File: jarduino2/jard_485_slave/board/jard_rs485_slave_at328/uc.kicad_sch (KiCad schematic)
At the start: 13 parts, among them J7 ISCP, U5 ATmega328P-A, Y1 Resonator

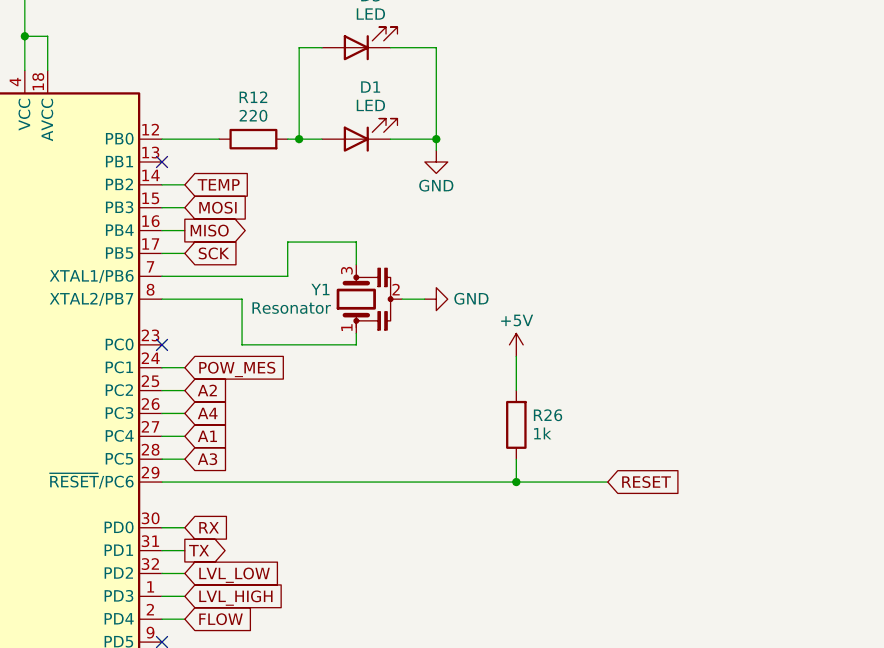
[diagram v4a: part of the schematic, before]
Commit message: Correction empreinte résonateur
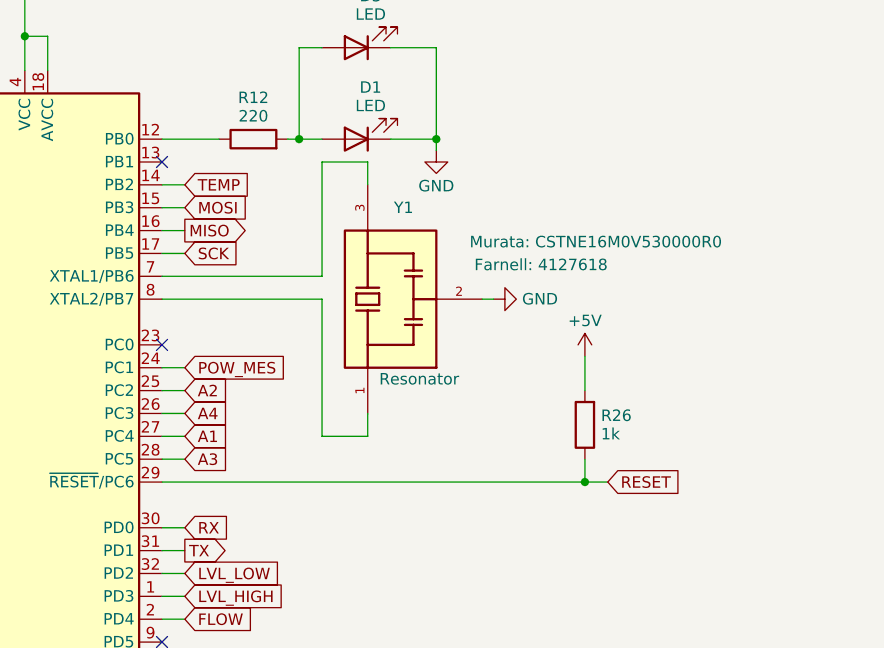
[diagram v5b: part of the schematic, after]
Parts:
- U5: Fabricant (none) -> Microchip: ATMEGA328P-AN; Fournisseur (none) -> Farnell: 2443178
- Y1: footprint Crystal:Resonator_SMD_Murata_CSTxExxV-3Pin_3.0x1.1mm_HandSoldering -> bpc:BPC_16MHz_CSTNE16M0V530000R0; symbol Device:Resonator -> bpc:BPC_16MHz_CSTNE16M0V530000R0; Availability (none) -> In Stock; Check_prices (none) -> https://www.snapeda.com/parts/CSTNE16M0V530000R0/Murata+Ele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; Fabricant (none) -> Murata: CSTNE16M0V530000R0; Fournisseur (none) -> Farnell: 4127618; MANUFACTURER (none) -> Murata; MAXIMUM_PACKAGE_HEIGHT (none) -> 1mm; MF (none) -> Murata Electronics; MP (none) -> CSTNE16M0V530000R0; PARTREV (none) -> JGC42-8853B; Package (none) -> SMD-3 Murata; Price (none) -> None; Purchase-URL (none) -> https://www.snapeda.com/api/url_track_click_mouser/?unipart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; STANDARD (none) -> Manufacturer Recomendations; SnapEDA_Link (none) -> https://www.snapeda.com/parts/CSTNE16M0V530000R0/Murata+Ele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
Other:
- moved on the sheet: R26

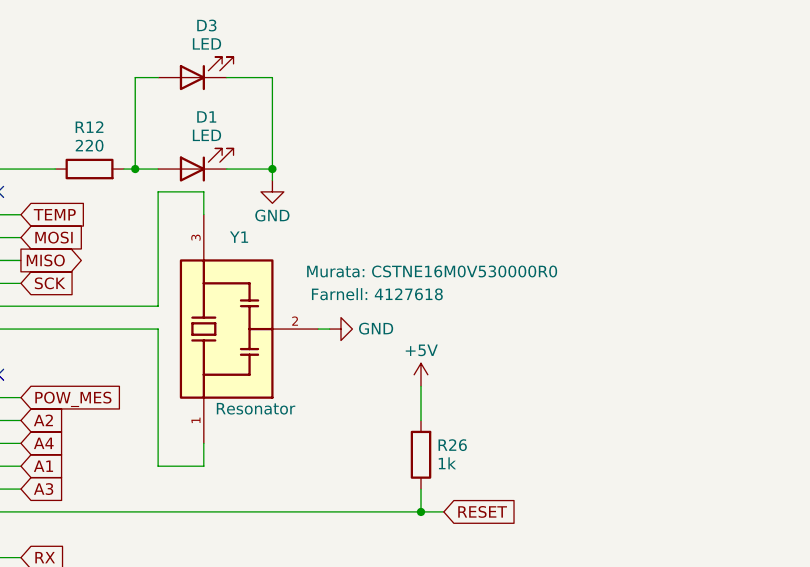
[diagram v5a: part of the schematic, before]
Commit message: Correction erreur de MOS (N au lieu de P) + Saisie complete de la BOM
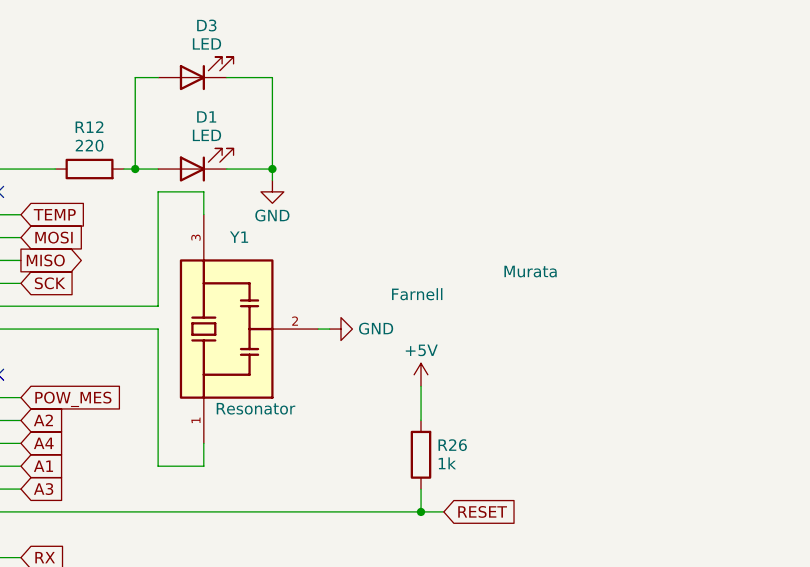
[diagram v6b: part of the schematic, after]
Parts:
- C? (x5): Fabricant (none) -> KEMET; Fournisseur (none) -> Farnell; RefFabricant (none) -> C0603X102J5GACAUTO; RefFournisseur (none) -> 2219417
- D1: Fabricant (none) -> ROHM; Fournisseur (none) -> Farnell; RefFabricant (none) -> SML-D14VWT86C; RefFournisseur (none) -> 2829438
- J7: Fabricant (none) -> AMPHENOL; Fournisseur (none) -> Farnell; RefFabricant (none) -> 95278-101-06LF; RefFournisseur (none) -> 3882224
- R12: Fabricant (none) -> MULTICOMP PRO; Fournisseur (none) -> Farnell; RefFabricant (none) -> MCMR06X224 JTL; RefFournisseur (none) -> 2073437
- R26: Fabricant (none) -> MULTICOMP PRO; Fournisseur (none) -> Farnell; RefFabricant (none) -> MC0100W060311K; RefFournisseur (none) -> 2845750
- U5: Fabricant Microchip: ATMEGA328P-AN -> Microchip; Fournisseur Farnell: 2443178 -> Farnell; RefFabricant (none) -> ATMEGA328P-AN; RefFournisseur (none) -> 2443178
- Y1: Fabricant Murata: CSTNE16M0V530000R0 -> Murata; Fournisseur Farnell: 4127618 -> Farnell; RefFabricant (none) -> CSTNE16M0V530000R0; RefFournisseur (none) -> 4127618
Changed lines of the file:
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@@
   (title_block
     (title "Carte de commande d'un OYA - Esclave RS485")
-    (date "2024-04-01")
-    (rev "D0")
+    (date "2024-04-02")
+    (rev "E0")
     (company "BPC")
     (comment 1 "Technologie CMS basée sur ATMEGA328")
@@
       (effects (font (size 1.27 1.27)) hide)
     )
+    (property "RefFabricant" "C0603X102J5GACAUTO" (at 109.22 95.25 0)
+      (effects (font (size 1.27 1.27)) hide)
+    )
+    (property "RefFournisseur" "2219417" (at 109.22 95.25 0)
+      (effects (font (size 1.27 1.27)) hide)
+    )
+    (property "Fabricant" "KEMET" (at 109.22 95.25 0)
+      (effects (font (size 1.27 1.27)) hide)
+    )
+    (property "Fournisseur" "Farnell" (at 109.22 95.25 0)
+      (effects (font (size 1.27 1.27)) hide)
+    )
+    (property "Description" "Condensateur céramique 100nF" (at 109.22 95.25 0)
+      (effects (font (size 1.27 1.27)) hide)
+    )
     (pin "1")
     (pin "2")
@@
     )
     (property "Datasheet" "~" (at 229.87 63.5 0)
+      (effects (font (size 1.27 1.27)) hide)
+    )
+    (property "RefFabricant" "95278-101-06LF" (at 229.87 63.5 0)
+      (effects (font (size 1.27 1.27)) hide)
+    )
+    (property "RefFournisseur" "3882224" (at 229.87 63.5 0)
+      (effects (font (size 1.27 1.27)) hide)
+    )
+    (property "Fabricant" "AMPHENOL" (at 229.87 63.5 0)
+      (effects (font (size 1.27 1.27)) hide)
+    )
+    (property "Fournisseur" "Farnell" (at 229.87 63.5 0)
+      (effects (font (size 1.27 1.27)) hide)
+    )
+    (property "Description" "Connecteur Header 6 broches" (at 229.87 63.5 0)
       (effects (font (size 1.27 1.27)) hide)
     )
@@
       (effects (font (size 1.27 1.27)) hide)
     )
+    (property "RefFabricant" "C0603X102J5GACAUTO" (at 143.51 69.85 0)
+      (effects (font (size 1.27 1.27)) hide)
+    )
+    (property "RefFournisseur" "2219417" (at 143.51 69.85 0)
+      (effects (font (size 1.27 1.27)) hide)
+    )
+    (property "Fabricant" "KEMET" (at 143.51 69.85 0)
+      (effects (font (size 1.27 1.27)) hide)
+    )
+    (property "Fournisseur" "Farnell" (at 143.51 69.85 0)
+      (effects (font (size 1.27 1.27)) hide)
+    )
+    (property "Description" "Condensateur céramique 100nF" (at 143.51 69.85 0)
+      (effects (font (size 1.27 1.27)) hide)
+    )
     (pin "1")
     (pin "2")
@@
       (effects (font (size 1.27 1.27)) hide)
     )
+    (property "RefFabricant" "C0603X102J5GACAUTO" (at 53.34 158.75 0)
+      (effects (font (size 1.27 1.27)) hide)
+    )
+    (property "RefFournisseur" "2219417" (at 53.34 158.75 0)
+      (effects (font (size 1.27 1.27)) hide)
+    )
+    (property "Fabricant" "KEMET" (at 53.34 158.75 0)
+      (effects (font (size 1.27 1.27)) hide)
+    )
+    (property "Fournisseur" "Farnell" (at 53.34 158.75 0)
+      (effects (font (size 1.27 1.27)) hide)
+    )
+    (property "Description" "Condensateur céramique 1nF" (at 53.34 158.75 0)
+      (effects (font (size 1.27 1.27)) hide)
+    )
     (pin "1")
     (pin "2")
@@
       (effects (font (size 1.27 1.27)) hide)
     )
+    (property "RefFabricant" "MC0100W060311K" (at 195.58 127 0)
+      (effects (font (size 1.27 1.27)) hide)
+    )
+    (property "RefFournisseur" "2845750" (at 195.58 127 0)
+      (effects (font (size 1.27 1.27)) hide)
+    )
+    (property "Fabricant" "MULTICOMP PRO" (at 195.58 127 0)
+      (effects (font (size 1.27 1.27)) hide)
+    )
+    (property "Fournisseur" "Farnell" (at 195.58 127 0)
+      (effects (font (size 1.27 1.27)) hide)
+    )
+    (property "Description" "Résistance 1kOhms" (at 195.58 127 0)
+      (effects (font (size 1.27 1.27)) hide)
+    )
     (pin "1")
     (pin "2")
@@
     )
     (property "Datasheet" "~" (at 170.18 95.25 0)
+      (effects (font (size 1.27 1.27)) hide)
+    )
+    (property "RefFabricant" "SML-D14VWT86C" (at 170.18 95.25 0)
+      (effects (font (size 1.27 1.27)) hide)
+    )
+    (property "RefFournisseur" "2829438" (at 170.18 95.25 0)
+      (effects (font (size 1.27 1.27)) hide)
+    )
+    (property "Fabricant" "ROHM" (at 170.18 95.25 0)
+      (effects (font (size 1.27 1.27)) hide)
+    )
+    (property "Fournisseur" "Farnell" (at 170.18 95.25 0)
+      (effects (font (size 1.27 1.27)) hide)
+    )
+    (property "Description" "LED rouge 805" (at 170.18 95.25 0)
       (effects (font (size 1.27 1.27)) hide)
     )
@@
       (effects (font (size 1.27 1.27)) hide)
     )
-    (property "Fabricant" "Murata: CSTNE16M0V530000R0" (at 210.82 106.68 90)
-      (effects (font (size 1.27 1.27)) (justify left))
-    )
-    (property "Fournisseur" "Farnell: 4127618" (at 198.12 109.22 90)
+    (property "Fabricant" "Murata" (at 210.82 106.68 90)
+      (effects (font (size 1.27 1.27)) (justify left))
+    )
+    (property "Fournisseur" "Farnell" (at 198.12 109.22 90)
       (effects (font (size 1.27 1.27)) (justify left))
     )
@@
       (effects (font (size 1.27 1.27)) (justify bottom) hide)
     )
-    (property "Description" "\n16 MHz Ceramic Resonator Built in Capacitor 15 pF ±0.3% 40 Ohms -40°C ~ 85°C Surface Mount\n" (at 173.99 113.03 0)
+    (property "Description" "Résonateur \n16 MHz / 15 pF" (at 173.99 113.03 0)
       (effects (font (size 1.27 1.27)) (justify bottom) hide)
     )
@@
     (property "MANUFACTURER" "Murata" (at 173.99 113.03 0)
       (effects (font (size 1.27 1.27)) (justify bottom) hide)
+    )
+    (property "RefFabricant" "CSTNE16M0V530000R0" (at 173.99 113.03 0)
+      (effects (font (size 1.27 1.27)) hide)
+    )
+    (property "RefFournisseur" "4127618" (at 173.99 113.03 0)
+      (effects (font (size 1.27 1.27)) hide)
     )
     (pin "1")
@@
     )
     (property "Datasheet" "" (at 49.53 161.29 0)
+      (effects (font (size 1.27 1.27)) hide)
+    )
+    (property "RefFabricant" "" (at 49.53 163.83 0)
+      (effects (font (size 1.27 1.27)) hide)
+    )
+    (property "RefFournisseur" "" (at 49.53 163.83 0)
+      (effects (font (size 1.27 1.27)) hide)
+    )
+    (property "Description" "Module de température Arduino" (at 49.53 163.83 0)
       (effects (font (size 1.27 1.27)) hide)
     )
@@
       (effects (font (size 1.27 1.27)) hide)
     )
-    (property "Fabricant" "Microchip: ATMEGA328P-AN" (at 133.35 125.73 0)
-      (effects (font (size 1.27 1.27)) hide)
-    )
-    (property "Fournisseur" "Farnell: 2443178" (at 133.35 125.73 0)
+    (property "Fabricant" "Microchip" (at 133.35 125.73 0)
+      (effects (font (size 1.27 1.27)) hide)
+    )
+    (property "Fournisseur" "Farnell" (at 133.35 125.73 0)
+      (effects (font (size 1.27 1.27)) hide)
+    )
+    (property "RefFabricant" "ATMEGA328P-AN" (at 133.35 125.73 0)
+      (effects (font (size 1.27 1.27)) hide)
+    )
+    (property "RefFournisseur" "2443178" (at 133.35 125.73 0)
+      (effects (font (size 1.27 1.27)) hide)
+    )
+    (property "Description" "Microcontrolleur ATMEGA328P" (at 133.35 125.73 0)
       (effects (font (size 1.27 1.27)) hide)
     )
@@
       (effects (font (size 1.27 1.27)) hide)
     )
+    (property "RefFabricant" "C0603X102J5GACAUTO" (at 143.51 58.42 0)
+      (effects (font (size 1.27 1.27)) hide)
+    )
+    (property "RefFournisseur" "2219417" (at 143.51 58.42 0)
+      (effects (font (size 1.27 1.27)) hide)
+    )
+    (property "Fabricant" "KEMET" (at 143.51 58.42 0)
+      (effects (font (size 1.27 1.27)) hide)
+    )
+    (property "Fournisseur" "Farnell" (at 143.51 58.42 0)
+      (effects (font (size 1.27 1.27)) hide)
+    )
+    (property "Description" "Condensateur céramique 1nF" (at 143.51 58.42 0)
+      (effects (font (size 1.27 1.27)) hide)
+    )
     (pin "1")
     (pin "2")
@@
       (effects (font (size 1.27 1.27)) hide)
     )
+    (property "RefFabricant" "C0603X102J5GACAUTO" (at 143.51 46.99 0)
+      (effects (font (size 1.27 1.27)) hide)
+    )
+    (property "RefFournisseur" "2219417" (at 143.51 46.99 0)
+      (effects (font (size 1.27 1.27)) hide)
+    )
+    (property "Fabricant" "KEMET" (at 143.51 46.99 0)
+      (effects (font (size 1.27 1.27)) hide)
+    )
+    (property "Fournisseur" "Farnell" (at 143.51 46.99 0)
+      (effects (font (size 1.27 1.27)) hide)
+    )
+    (property "Description" "Condensateur céramique 100nF" (at 143.51 46.99 0)
+      (effects (font (size 1.27 1.27)) hide)
+    )
     (pin "1")
     (pin "2")
@@
       (effects (font (size 1.27 1.27)) hide)
     )
+    (property "RefFabricant" "MCMR06X224 JTL" (at 158.75 95.25 0)
+      (effects (font (size 1.27 1.27)) hide)
+    )
+    (property "RefFournisseur" "2073437" (at 158.75 95.25 0)
+      (effects (font (size 1.27 1.27)) hide)
+    )
+    (property "Fabricant" "MULTICOMP PRO" (at 158.75 95.25 0)
+      (effects (font (size 1.27 1.27)) hide)
+    )
+    (property "Fournisseur" "Farnell" (at 158.75 95.25 0)
+      (effects (font (size 1.27 1.27)) hide)
+    )
+    (property "Description" "Résistance 220 Ohms" (at 158.75 95.25 0)
+      (effects (font (size 1.27 1.27)) hide)
+    )
     (pin "1")
     (pin "2")
@@
       (effects (font (size 1.27 1.27)) hide)
     )
+    (property "RefFabricant" "" (at 170.18 85.09 0)
+      (effects (font (size 1.27 1.27)) hide)
+    )
+    (property "RefFournisseur" "" (at 170.18 85.09 0)
+      (effects (font (size 1.27 1.27)) hide)
+    )
+    (property "Description" "LED rouge 3mm" (at 170.18 85.09 0)
+      (effects (font (size 1.27 1.27)) hide)
+    )

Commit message: Ajout des prix des composants
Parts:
- C? (x5): Price (none) -> 0,42
- D1: Price (none) -> 0,4992
- D3: Fabricant (none) -> MULTICOMP PRO; Fournisseur (none) -> Farnell; Price (none) -> 3,78; RefFabricant (none) -> MP000451; RefFournisseur (none) -> 3130206
- J7: Price (none) -> 0,5748
- R12: Price (none) -> 0,009
- R26: Price (none) -> 0,0036
- U5: Price (none) -> 3,12
- U?: Fournisseur (none) -> Ali express; Price (none) -> 0,635; Purchase-URL (none) -> https://fr.aliexpress.com/item/1005005046929046.html?spm=a2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; RefFournisseur (none) -> DTH22
- Y1: Price None -> 0,2616
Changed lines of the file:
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@@
+      (effects (font (size 1.27 1.27)) hide)
+    )
+    (property "Price" "0,42" (at 109.22 95.25 0)
       (effects (font (size 1.27 1.27)) hide)
     )
@@
     )
     (property "Description" "Connecteur Header 6 broches" (at 229.87 63.5 0)
+      (effects (font (size 1.27 1.27)) hide)
+    )
+    (property "Price" "0,5748" (at 229.87 63.5 0)
       (effects (font (size 1.27 1.27)) hide)
     )
@@
       (effects (font (size 1.27 1.27)) hide)
     )
+    (property "Price" "0,42" (at 143.51 69.85 0)
+      (effects (font (size 1.27 1.27)) hide)
+    )
     (pin "1")
     (pin "2")
@@
       (effects (font (size 1.27 1.27)) hide)
     )
+    (property "Price" "0,42" (at 53.34 158.75 0)
+      (effects (font (size 1.27 1.27)) hide)
+    )
     (pin "1")
     (pin "2")
@@
       (effects (font (size 1.27 1.27)) hide)
     )
+    (property "Price" "0,0036" (at 195.58 127 0)
+      (effects (font (size 1.27 1.27)) hide)
+    )
     (pin "1")
     (pin "2")
@@
     )
     (property "Description" "LED rouge 805" (at 170.18 95.25 0)
+      (effects (font (size 1.27 1.27)) hide)
+    )
+    (property "Price" "0,4992" (at 170.18 95.25 0)
       (effects (font (size 1.27 1.27)) hide)
     )
@@
       (effects (font (size 1.27 1.27)) (justify bottom) hide)
     )
-    (property "Price" "None" (at 173.99 113.03 0)
+    (property "Price" "0,2616" (at 173.99 113.03 0)
       (effects (font (size 1.27 1.27)) (justify bottom) hide)
     )
@@
       (effects (font (size 1.27 1.27)) hide)
     )
-    (property "RefFournisseur" "" (at 49.53 163.83 0)
+    (property "RefFournisseur" "DTH22" (at 49.53 163.83 0)
       (effects (font (size 1.27 1.27)) hide)
     )
     (property "Description" "Module de température Arduino" (at 49.53 163.83 0)
+      (effects (font (size 1.27 1.27)) hide)
+    )
+    (property "Fournisseur" "Ali express" (at 49.53 163.83 0)
+      (effects (font (size 1.27 1.27)) hide)
+    )
+    (property "Price" "0,635" (at 49.53 163.83 0)
+      (effects (font (size 1.27 1.27)) hide)
+    )
+    (property "Purchase-URL" "https://fr.aliexpress.com/item/1005005046929046.html?spm=a2g0o.productlist.main.1.6bc358cfkBpnLN&algo_pvid=d68faa62-b15e-4a60-b378-f75477d8c492&algo_exp_id=d68faa62-b15e-4a60-b378-f75477d8c492-0&pdp_npi=4%40dis%21EUR%216.35%216.35%21%21%216.72%216.72%21%40210386d117123955551348030ebc5b%2112000031442655490%21sea%21FR%212150986022%21&curPageLogUid=S3wz0qZbaH38&utparam-url=scene%3Asearch%7Cquery_from%3A" (at 49.53 163.83 0)
       (effects (font (size 1.27 1.27)) hide)
     )
@@
     )
     (property "Description" "Microcontrolleur ATMEGA328P" (at 133.35 125.73 0)
+      (effects (font (size 1.27 1.27)) hide)
+    )
+    (property "Price" "3,12" (at 133.35 125.73 0)
       (effects (font (size 1.27 1.27)) hide)
     )
@@
       (effects (font (size 1.27 1.27)) hide)
     )
+    (property "Price" "0,42" (at 143.51 58.42 0)
+      (effects (font (size 1.27 1.27)) hide)
+    )
     (pin "1")
     (pin "2")
@@
       (effects (font (size 1.27 1.27)) hide)
     )
+    (property "Price" "0,42" (at 143.51 46.99 0)
+      (effects (font (size 1.27 1.27)) hide)
+    )
     (pin "1")
     (pin "2")
@@
       (effects (font (size 1.27 1.27)) hide)
     )
+    (property "Price" "0,009" (at 158.75 95.25 0)
+      (effects (font (size 1.27 1.27)) hide)
+    )
     (pin "1")
     (pin "2")
@@
       (effects (font (size 1.27 1.27)) hide)
     )
-    (property "RefFabricant" "" (at 170.18 85.09 0)
-      (effects (font (size 1.27 1.27)) hide)
-    )
-    (property "RefFournisseur" "" (at 170.18 85.09 0)
+    (property "RefFabricant" "MP000451" (at 170.18 85.09 0)
+      (effects (font (size 1.27 1.27)) hide)
+    )
+    (property "RefFournisseur" "3130206" (at 170.18 85.09 0)
       (effects (font (size 1.27 1.27)) hide)
     )
@@
       (effects (font (size 1.27 1.27)) hide)
     )
+    (property "Fabricant" "MULTICOMP PRO" (at 170.18 85.09 0)
+      (effects (font (size 1.27 1.27)) hide)
+    )
+    (property "Fournisseur" "Farnell" (at 170.18 85.09 0)
+      (effects (font (size 1.27 1.27)) hide)
+    )
+    (property "Price" "3,78" (at 170.18 85.09 0)
+      (effects (font (size 1.27 1.27)) hide)
+    )
